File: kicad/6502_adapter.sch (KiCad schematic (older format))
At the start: 23 parts, among them P1 CONN_02X20, P2 CONN_02X20, P3 CONN_01X03, P4 CONN_01X02, U1 WD65C02, U2 74LVC4245, U3 74LVC4245, U4 74LVC4245, U5 74LVC4245, U6 74LVC4245

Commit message: PCB: Migrated to KiCad 5.0
Change-Id: Ib035c47ddc7768d46feebc4e1ea05c04dbd125a6
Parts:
- C1, C10, C11, C2, C3, C4, C5, C7, C8, C9: symbol C_Small -> 6502_adapter-rescue:C_Small
- C12, C6: symbol CP1_Small -> 6502_adapter-rescue:CP1_Small
- P1, P2: symbol CONN_02X20 -> 6502_adapter-rescue:CONN_02X20
- P3: symbol CONN_01X03 -> 6502_adapter-rescue:CONN_01X03
- P4: symbol CONN_01X02 -> 6502_adapter-rescue:CONN_01X02
- R1: symbol R_Small -> 6502_adapter-rescue:R_Small
- U1: symbol WD65C02 -> 65xx:WD65C02
- U2, U3, U4, U5, U6: symbol 74LVC8T245 -> 74lvc:74LVC8T245
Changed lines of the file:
@@
-EESchema Schematic File Version 2
-LIBS:power
-LIBS:device
-LIBS:transistors
-LIBS:conn
-LIBS:linear
-LIBS:regul
-LIBS:74xx
-LIBS:cmos4000
-LIBS:adc-dac
-LIBS:memory
-LIBS:xilinx
-LIBS:microcontrollers
-LIBS:dsp
-LIBS:microchip
-LIBS:analog_switches
-LIBS:motorola
-LIBS:texas
-LIBS:intel
-LIBS:audio
-LIBS:interface
-LIBS:digital-audio
-LIBS:philips
-LIBS:display
-LIBS:cypress
-LIBS:siliconi
-LIBS:opto
-LIBS:atmel
-LIBS:contrib
-LIBS:valves
-LIBS:65xx
-LIBS:74lvc
-EELAYER 25 0
+EESchema Schematic File Version 4
+LIBS:6502_adapter-cache
+EELAYER 26 0
 EELAYER END
 $Descr A4 11693 8268
@@
 $EndDescr
 $Comp
-L WD65C02 U1
+L 65xx:WD65C02 U1
 U 1 1 5975BF41
 P 5800 3600
@@
 $EndComp
 $Comp
-L 74LVC8T245 U4
+L 74lvc:74LVC8T245 U4
 U 1 1 5975C5CE
 P 3650 5600
@@
 $EndComp
 $Comp
-L CONN_02X20 P2
+L 6502_adapter-rescue:CONN_02X20 P2
 U 1 1 5975C737
 P 1200 4100
@@
 $EndComp
 $Comp
-L CONN_02X20 P1
+L 6502_adapter-rescue:CONN_02X20 P1
 U 1 1 5975C7A4
 P 10450 3950
@@
 $EndComp
 $Comp
-L 74LVC8T245 U5
+L 74lvc:74LVC8T245 U5
 U 1 1 5975C870
 P 8100 3750
@@
 $EndComp
 $Comp
-L 74LVC8T245 U2
+L 74lvc:74LVC8T245 U2
 U 1 1 5975C8C1
 P 3300 1650
@@
 $EndComp
 $Comp
-L 74LVC8T245 U3
+L 74lvc:74LVC8T245 U3
 U 1 1 5975C914
 P 3250 3850
@@
 $EndComp
 $Comp
-L 74LVC8T245 U6
+L 74lvc:74LVC8T245 U6
 U 1 1 5975C957
 P 8100 1950
@@
 NoConn ~ 6450 3200
 $Comp
-L CONN_01X03 P3
+L 6502_adapter-rescue:CONN_01X03 P3
 U 1 1 59760CE2
 P 5150 1050
@@
 GND
 $Comp
-L CONN_01X02 P4
+L 6502_adapter-rescue:CONN_01X02 P4
 U 1 1 5976110F
 P 4300 2850
@@
 LV_SYNC
 $Comp
-L R_Small R1
+L 6502_adapter-rescue:R_Small R1
 U 1 1 59761BB3
 P 7050 1100
@@
 5V
 $Comp
-L C_Small C1
+L 6502_adapter-rescue:C_Small C1
 U 1 1 597620E8
 P 1100 6900
@@
 $EndComp
 $Comp
-L C_Small C2
+L 6502_adapter-rescue:C_Small C2
 U 1 1 5976220A
 P 1400 6900
@@
 $EndComp
 $Comp
-L C_Small C3
+L 6502_adapter-rescue:C_Small C3
 U 1 1 59762254
 P 1700 6900
@@
 $EndComp
 $Comp
-L C_Small C4
+L 6502_adapter-rescue:C_Small C4
 U 1 1 59762296
 P 2000 6900
@@
 $EndComp
 $Comp
-L C_Small C5
+L 6502_adapter-rescue:C_Small C5
 U 1 1 597622DF
 P 2300 6900
@@
 $EndComp
 $Comp
-L C_Small C7
+L 6502_adapter-rescue:C_Small C7
 U 1 1 597624D7
 P 3250 6900
@@
 $EndComp
 $Comp
-L C_Small C8
+L 6502_adapter-rescue:C_Small C8
 U 1 1 5976252A
 P 3550 6900
@@
 $EndComp
 $Comp
-L C_Small C9
+L 6502_adapter-rescue:C_Small C9
 U 1 1 59762588
 P 3850 6900
@@
 $EndComp
 $Comp
-L C_Small C10
+L 6502_adapter-rescue:C_Small C10
 U 1 1 597625E5
 P 4150 6900
@@
 $EndComp
 $Comp
-L C_Small C11
+L 6502_adapter-rescue:C_Small C11
 U 1 1 59762645
 P 4450 6900
@@
 $EndComp
 $Comp
-L CP1_Small C6
+L 6502_adapter-rescue:CP1_Small C6
 U 1 1 597630BE
 P 2600 6900
@@
 $EndComp
 $Comp
-L CP1_Small C12
+L 6502_adapter-rescue:CP1_Small C12
 U 1 1 59763501
 P 4750 6900
@@
 NoConn ~ 1450 3250
 $Comp
-L PWR_FLAG #FLG01
+L power:PWR_FLAG #FLG01
 U 1 1 597673C3
 P 1100 6700
@@
 $EndComp
 $Comp
-L PWR_FLAG #FLG02
+L power:PWR_FLAG #FLG02
 U 1 1 59767405
 P 3250 6700
@@
 $EndComp
 $Comp
-L PWR_FLAG #FLG03
+L power:PWR_FLAG #FLG03
 U 1 1 59767675
 P 800 7100
@@
 	4950 1700 4000 1700
 Wire Wire Line
-	6450 3300 7400 3300
+	6450 3300 6650 3300
 Wire Wire Line
 	5150 3300 4550 3300
@@
 	1100 7000 1100 7100
 Wire Wire Line
-	800  7100 4750 7100
+	800  7100 1100 7100
 Wire Wire Line
 	4450 7100 4450 7000
@@
 Wire Wire Line
 	3850 7000 3850 7100
-Wire Wire Line
-	3850 7100 3900 7100
-Connection ~ 3900 7100
+Connection ~ 3850 7100
 Wire Wire Line
 	3550 7000 3550 7100
@@
 	1100 6800 1100 6700
 Wire Wire Line
-	1100 6700 2600 6700
+	1100 6700 1400 6700
 Wire Wire Line
 	2300 6700 2300 6800
@@
 	3250 6800 3250 6700
 Wire Wire Line
-	3250 6700 4750 6700
+	3250 6700 3550 6700
 Wire Wire Line
 	4450 6700 4450 6800
@@
 Wire Wire Line
 	5150 5950 4350 5950
+Wire Wire Line
+	6650 3300 7400 3300
+Wire Wire Line
+	4150 7100 4450 7100
+Wire Wire Line
+	3250 7100 3550 7100
+Wire Wire Line
+	2300 7100 2600 7100
+Wire Wire Line
+	2000 7100 2300 7100
+Wire Wire Line
+	1700 7100 2000 7100
+Wire Wire Line
+	1400 7100 1700 7100
+Wire Wire Line
+	2000 6700 2300 6700
+Wire Wire Line
+	1700 6700 2000 6700
+Wire Wire Line
+	1400 6700 1700 6700
+Wire Wire Line
+	4150 6700 4450 6700
+Wire Wire Line
+	3850 6700 4150 6700
+Wire Wire Line
+	3550 6700 3850 6700
+Wire Wire Line
+	2300 6700 2600 6700
+Wire Wire Line
+	2600 7100 3250 7100
+Wire Wire Line
+	4450 6700 4750 6700
+Wire Wire Line
+	4450 7100 4750 7100
+Wire Wire Line
+	1100 7100 1400 7100
+Wire Wire Line
+	3550 7100 4150 7100
 $EndSCHEMATC

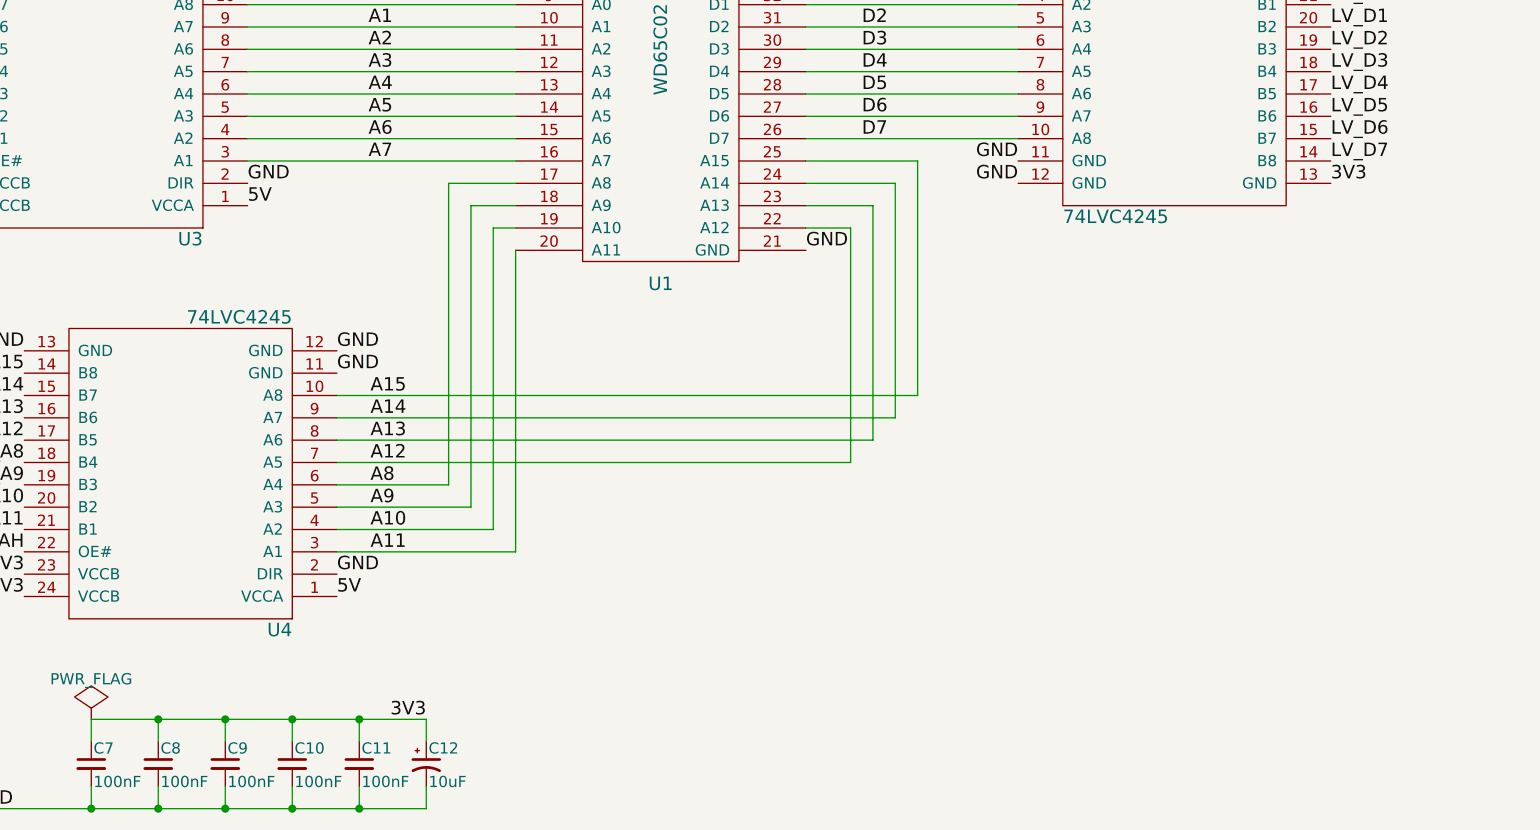
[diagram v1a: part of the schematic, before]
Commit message: Updated to kicad 5.1.4
Change-Id: Ie4dcf4e2a2838c19be82e0fb09b6ff49b04564ac
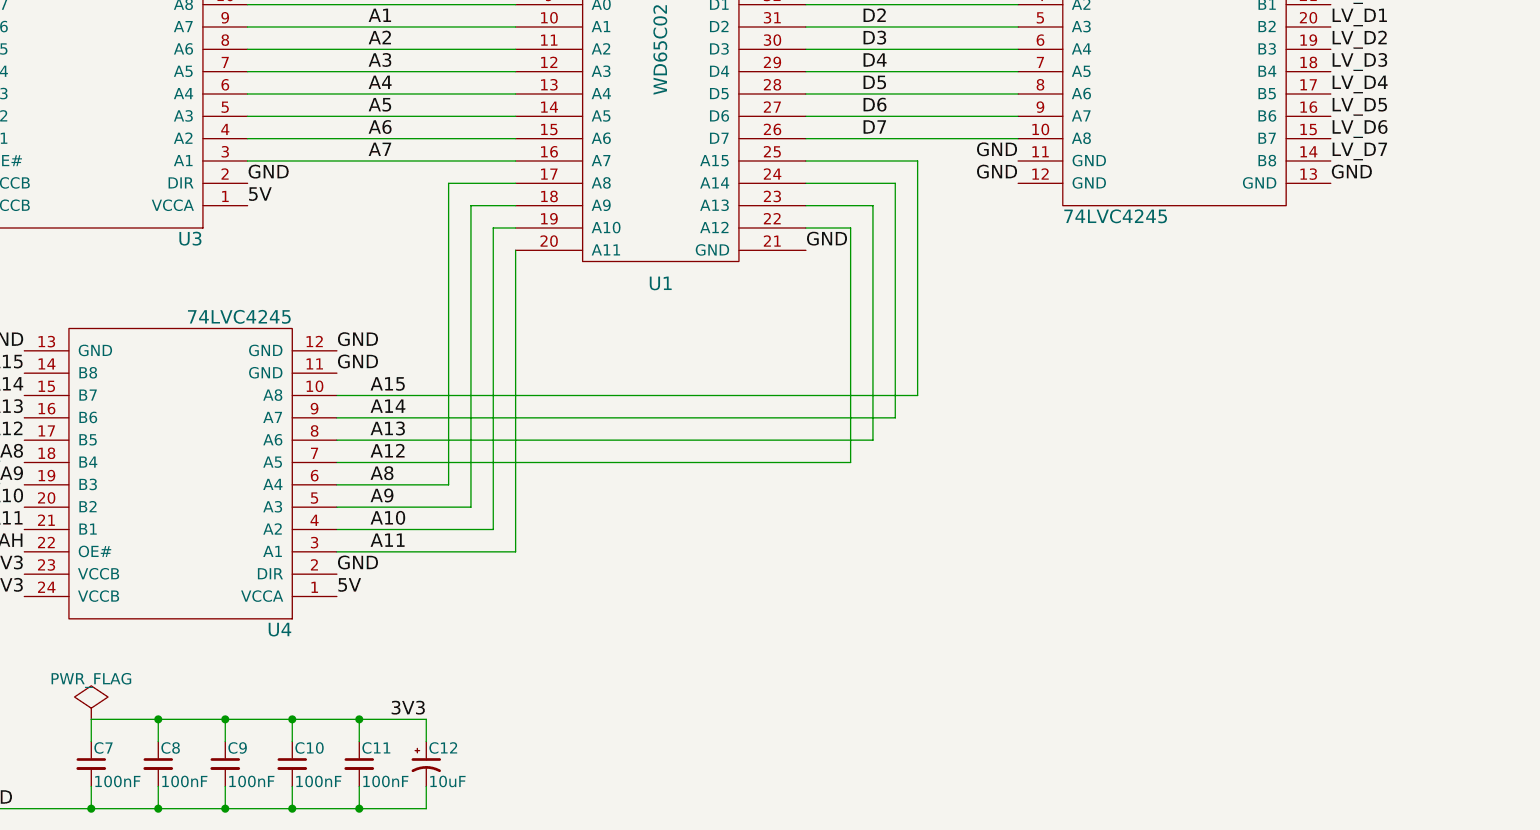
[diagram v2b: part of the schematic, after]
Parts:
- C1, C10, C11, C12, C2, C3, C4, C5, C6, C7, C8, C9: footprint Capacitors_SMD:C_0805_HandSoldering -> Capacitor_SMD:C_0805_2012Metric_Pad1.15x1.40mm_HandSolder
- R1: footprint Capacitors_SMD:C_0805_HandSoldering -> Resistor_SMD:R_0805_2012Metric_Pad1.15x1.40mm_HandSolder
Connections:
- net 3V3: no longer U5.13 (GND)
- net GND: now also U5.13 (GND)
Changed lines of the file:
@@
 EESchema Schematic File Version 4
 LIBS:6502_adapter-cache
-EELAYER 26 0
+EELAYER 30 0
 EELAYER END
 $Descr A4 11693 8268
@@
 Text Label 5150 3400 2    60   ~ 0
 5V
-Text Label 8800 4300 0    60   ~ 0
-3V3
 Text Label 4500 5650 0    60   ~ 0
 A8
@@
 F 0 "R1" H 7080 1120 50  0000 L CNN
 F 1 "4K7" H 7080 1060 50  0000 L CNN
-F 2 "Capacitors_SMD:C_0805_HandSoldering" H 7050 1100 50  0001 C CNN
+F 2 "Resistor_SMD:R_0805_2012Metric_Pad1.15x1.40mm_HandSolder" H 7050 1100 50  0001 C CNN
 F 3 "" H 7050 1100 50  0000 C CNN
 	1    7050 1100
@@
 F 0 "C1" H 1110 6970 50  0000 L CNN
 F 1 "100nF" H 1110 6820 50  0000 L CNN
-F 2 "Capacitors_SMD:C_0805_HandSoldering" H 1100 6900 50  0001 C CNN
+F 2 "Capacitor_SMD:C_0805_2012Metric_Pad1.15x1.40mm_HandSolder" H 1100 6900 50  0001 C CNN
 F 3 "" H 1100 6900 50  0000 C CNN
 	1    1100 6900
@@
 F 0 "C2" H 1410 6970 50  0000 L CNN
 F 1 "100nF" H 1410 6820 50  0000 L CNN
-F 2 "Capacitors_SMD:C_0805_HandSoldering" H 1400 6900 50  0001 C CNN
+F 2 "Capacitor_SMD:C_0805_2012Metric_Pad1.15x1.40mm_HandSolder" H 1400 6900 50  0001 C CNN
 F 3 "" H 1400 6900 50  0000 C CNN
 	1    1400 6900
@@
 F 0 "C3" H 1710 6970 50  0000 L CNN
 F 1 "100nF" H 1710 6820 50  0000 L CNN
-F 2 "Capacitors_SMD:C_0805_HandSoldering" H 1700 6900 50  0001 C CNN
+F 2 "Capacitor_SMD:C_0805_2012Metric_Pad1.15x1.40mm_HandSolder" H 1700 6900 50  0001 C CNN
 F 3 "" H 1700 6900 50  0000 C CNN
 	1    1700 6900
@@
 F 0 "C4" H 2010 6970 50  0000 L CNN
 F 1 "100nF" H 2010 6820 50  0000 L CNN
-F 2 "Capacitors_SMD:C_0805_HandSoldering" H 2000 6900 50  0001 C CNN
+F 2 "Capacitor_SMD:C_0805_2012Metric_Pad1.15x1.40mm_HandSolder" H 2000 6900 50  0001 C CNN
 F 3 "" H 2000 6900 50  0000 C CNN
 	1    2000 6900
@@
 F 0 "C5" H 2310 6970 50  0000 L CNN
 F 1 "100nF" H 2310 6820 50  0000 L CNN
-F 2 "Capacitors_SMD:C_0805_HandSoldering" H 2300 6900 50  0001 C CNN
+F 2 "Capacitor_SMD:C_0805_2012Metric_Pad1.15x1.40mm_HandSolder" H 2300 6900 50  0001 C CNN
 F 3 "" H 2300 6900 50  0000 C CNN
 	1    2300 6900
@@
 F 0 "C7" H 3260 6970 50  0000 L CNN
 F 1 "100nF" H 3260 6820 50  0000 L CNN
-F 2 "Capacitors_SMD:C_0805_HandSoldering" H 3250 6900 50  0001 C CNN
+F 2 "Capacitor_SMD:C_0805_2012Metric_Pad1.15x1.40mm_HandSolder" H 3250 6900 50  0001 C CNN
 F 3 "" H 3250 6900 50  0000 C CNN
 	1    3250 6900
@@
 F 0 "C8" H 3560 6970 50  0000 L CNN
 F 1 "100nF" H 3560 6820 50  0000 L CNN
-F 2 "Capacitors_SMD:C_0805_HandSoldering" H 3550 6900 50  0001 C CNN
+F 2 "Capacitor_SMD:C_0805_2012Metric_Pad1.15x1.40mm_HandSolder" H 3550 6900 50  0001 C CNN
 F 3 "" H 3550 6900 50  0000 C CNN
 	1    3550 6900
@@
 F 0 "C9" H 3860 6970 50  0000 L CNN
 F 1 "100nF" H 3860 6820 50  0000 L CNN
-F 2 "Capacitors_SMD:C_0805_HandSoldering" H 3850 6900 50  0001 C CNN
+F 2 "Capacitor_SMD:C_0805_2012Metric_Pad1.15x1.40mm_HandSolder" H 3850 6900 50  0001 C CNN
 F 3 "" H 3850 6900 50  0000 C CNN
 	1    3850 6900
@@
 F 0 "C10" H 4160 6970 50  0000 L CNN
 F 1 "100nF" H 4160 6820 50  0000 L CNN
-F 2 "Capacitors_SMD:C_0805_HandSoldering" H 4150 6900 50  0001 C CNN
+F 2 "Capacitor_SMD:C_0805_2012Metric_Pad1.15x1.40mm_HandSolder" H 4150 6900 50  0001 C CNN
 F 3 "" H 4150 6900 50  0000 C CNN
 	1    4150 6900
@@
 F 0 "C11" H 4460 6970 50  0000 L CNN
 F 1 "100nF" H 4460 6820 50  0000 L CNN
-F 2 "Capacitors_SMD:C_0805_HandSoldering" H 4450 6900 50  0001 C CNN
+F 2 "Capacitor_SMD:C_0805_2012Metric_Pad1.15x1.40mm_HandSolder" H 4450 6900 50  0001 C CNN
 F 3 "" H 4450 6900 50  0000 C CNN
 	1    4450 6900
@@
 F 0 "C6" H 2610 6970 50  0000 L CNN
 F 1 "10uF" H 2610 6820 50  0000 L CNN
-F 2 "Capacitors_SMD:C_0805_HandSoldering" H 2600 6900 50  0001 C CNN
+F 2 "Capacitor_SMD:C_0805_2012Metric_Pad1.15x1.40mm_HandSolder" H 2600 6900 50  0001 C CNN
 F 3 "" H 2600 6900 50  0000 C CNN
 	1    2600 6900
@@
 F 0 "C12" H 4760 6970 50  0000 L CNN
 F 1 "10uF" H 4760 6820 50  0000 L CNN
-F 2 "Capacitors_SMD:C_0805_HandSoldering" H 4750 6900 50  0001 C CNN
+F 2 "Capacitor_SMD:C_0805_2012Metric_Pad1.15x1.40mm_HandSolder" H 4750 6900 50  0001 C CNN
 F 3 "" H 4750 6900 50  0000 C CNN
 	1    4750 6900
@@
 	1100 7100 1400 7100
 Wire Wire Line
-	3550 7100 4150 7100
+	3550 7100 3850 7100
+Wire Wire Line
+	3850 7100 4150 7100
+Text Label 8800 4300 0    60   ~ 0
+GND
 $EndSCHEMATC
